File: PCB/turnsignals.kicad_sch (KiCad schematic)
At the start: 22 parts

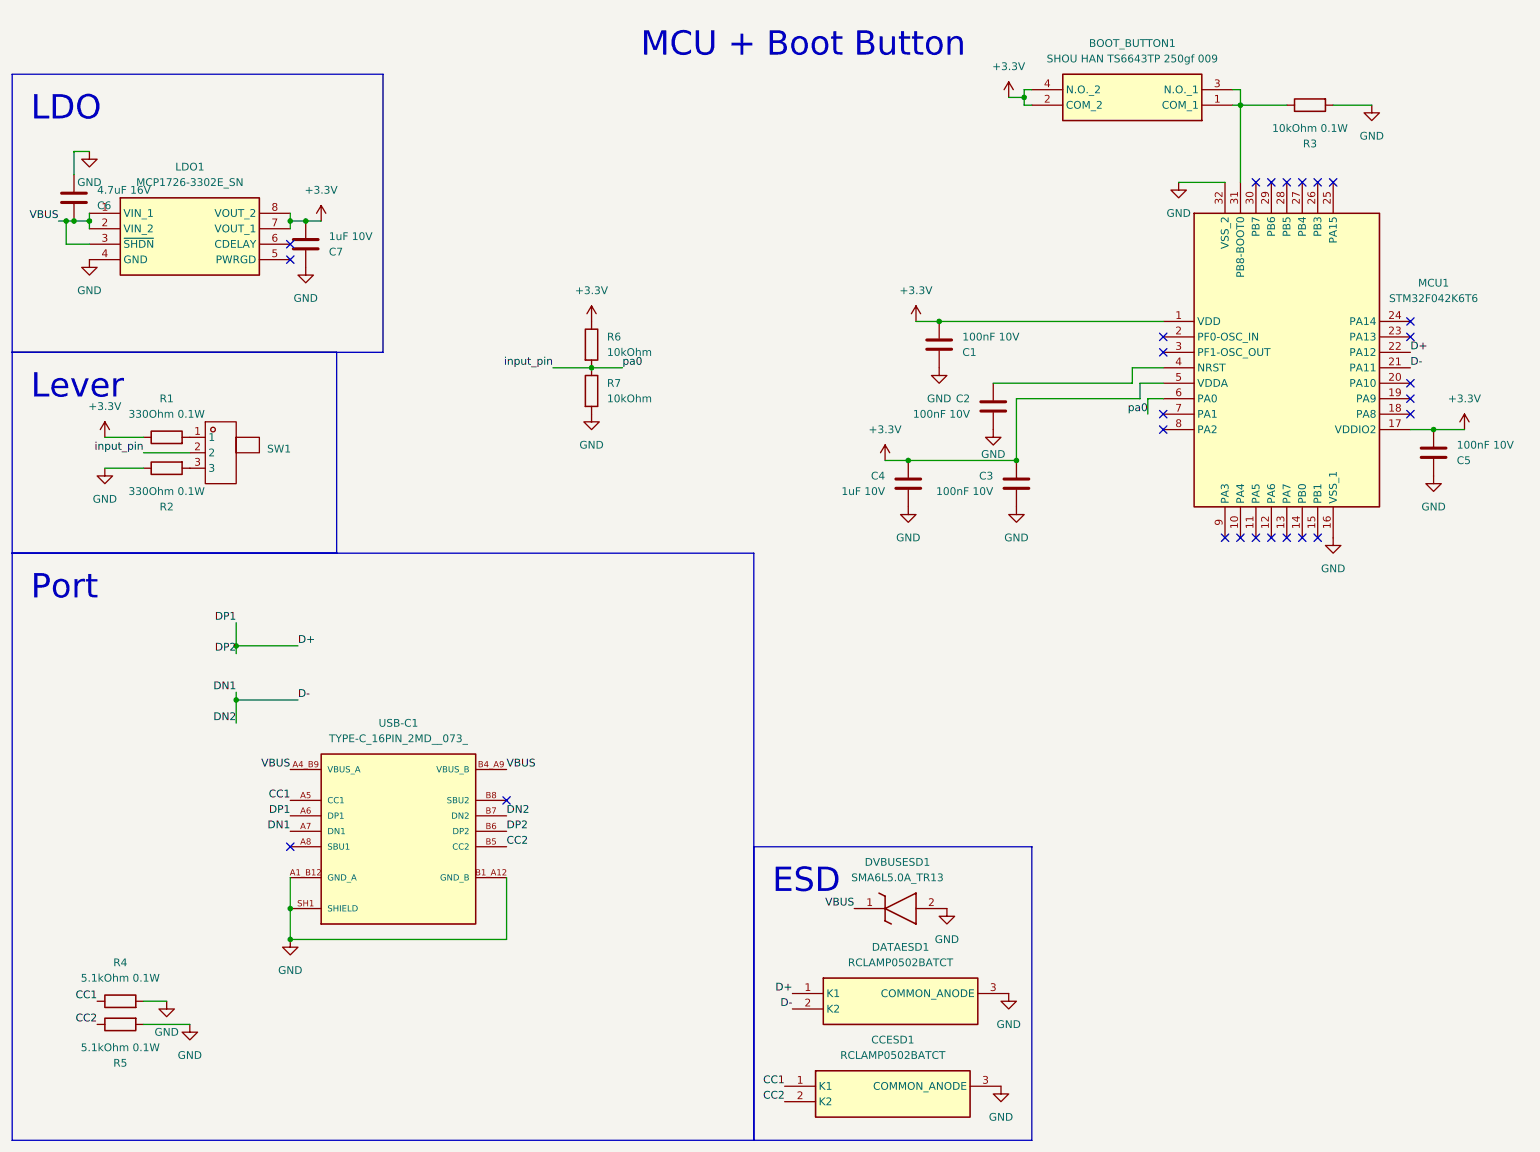
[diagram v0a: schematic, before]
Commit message: Corrected button wiring
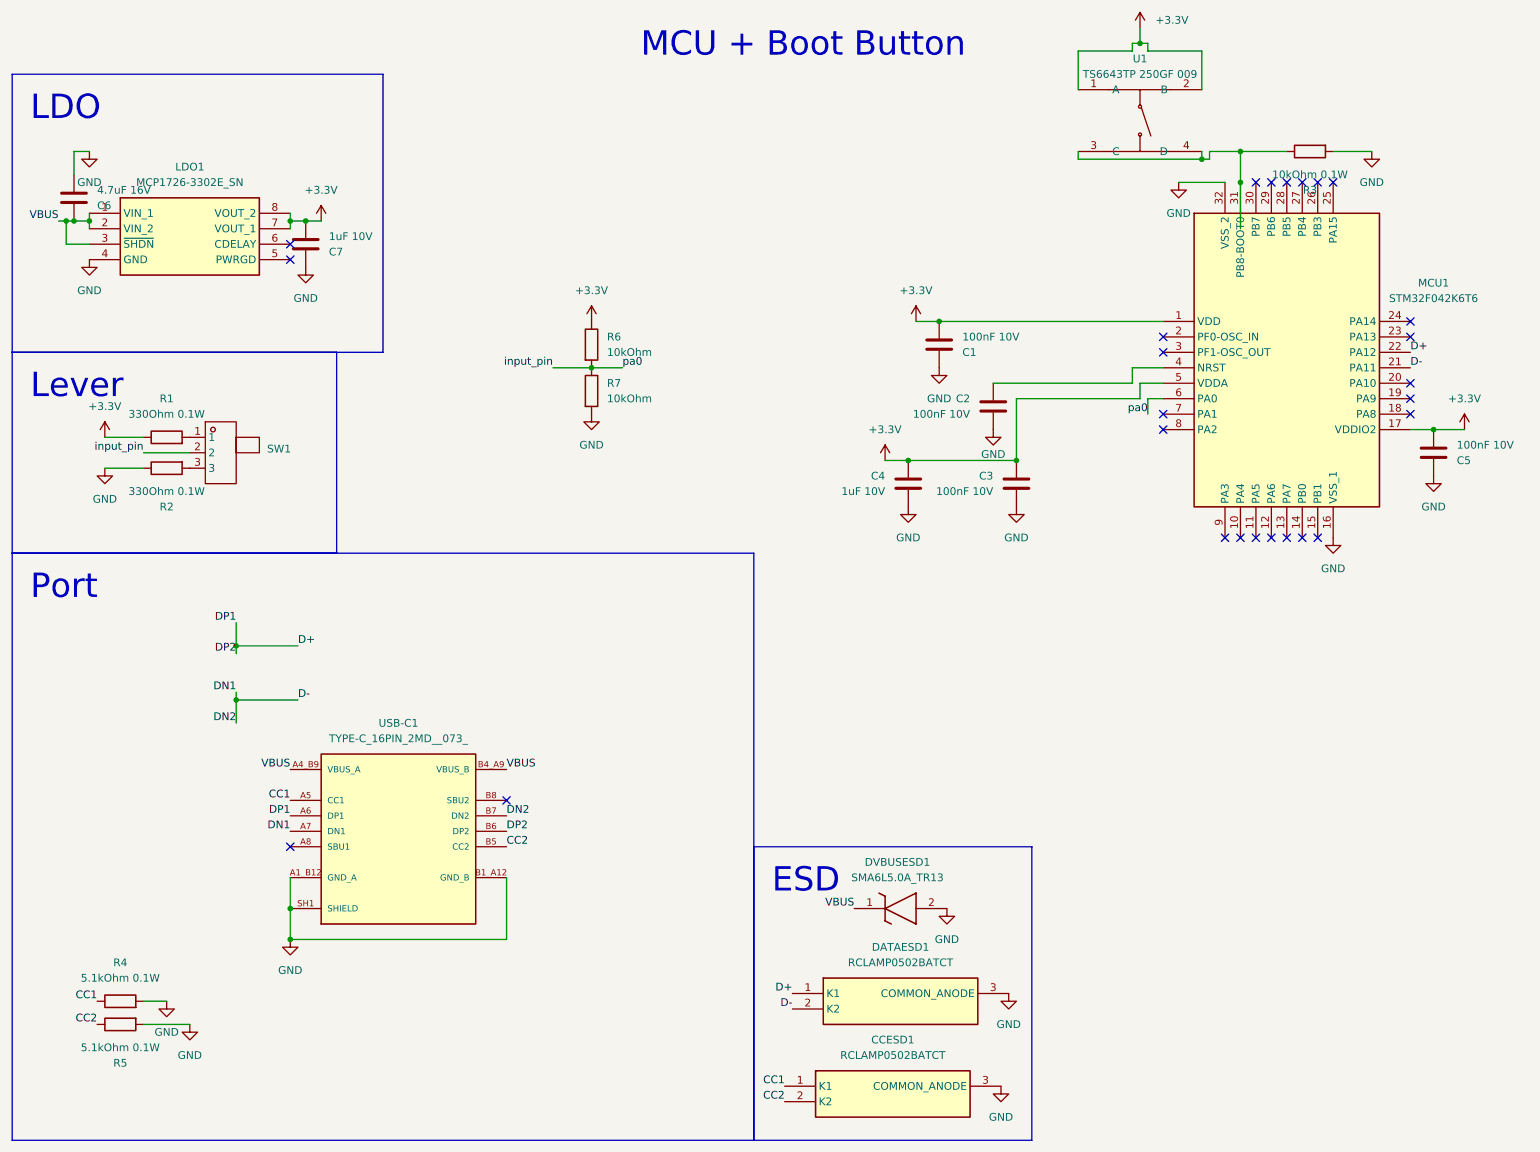
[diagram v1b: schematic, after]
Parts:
- removed BOOT_BUTTON1: SHOU HAN TS6643TP 250gf 009, SamacSys_Parts:TS406643BK160SMTTR, symbol REQUIRED:TS40-66-43-BK-160-SMT-TR
- added U1: TS6643TP 250GF 009, easyeda2kicad:SW-SMD_4P-L6.2-W6.0-P4.50-LS9.0, symbol REQUIRED:TS6643TP250GF009
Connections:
- net +3.3V: now also U1.1 (A), U1.2 (B)
- net at MCU1.31 (PB8-BOOT0), R3.1: now also U1.3 (C), U1.4 (D)
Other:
- moved on the sheet: R3
